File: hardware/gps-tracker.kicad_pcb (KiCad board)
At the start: 4 copper layers, 83 parts, among them J1 USB_B_Micro, J2 Conn_01x07, J3 Conn_01x08, J4 Conn_01x03, J5 Conn_01x04, SW1 SW_Push, SW2 SW_Push, SW3 SW_Push, SW4 SW_Push, SW5 SW_Push, SW6 SW_DPDT_x2, U1 STM32G070KBTx, U2 CH340C, U3 LTR-303ALS-01, U4 MIC5365-3.3YD5, U5 LIS2MDLTR, U6 LC86LICMD, U7 E22-900T30S, U8 TP4056

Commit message: First pass at PCB positions
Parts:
- removed H4: MountingHole, MountingHole:MountingHole_3.2mm_M3
- added C16: 470uF, Homebrew:CP_Radial_D6.3mm_P2.50mm_470uF, B.Cu at (123.1, 103.8)
- added C19: 470uF, Homebrew:CP_Radial_D6.3mm_P2.50mm_470uF, B.Cu at (122.8, 115.8)
- added C34: 10uF, Capacitor_SMD:C_0603_1608Metric, B.Cu at (131.7, 63.5)
- added C35: 10uF, Capacitor_SMD:C_0603_1608Metric, B.Cu at (85.8, 106.7)
- added C36: 100nF, Capacitor_SMD:C_0402_1005Metric, B.Cu at (137.3, 63.0)
- added C37: 47uF, Capacitor_SMD:C_1206_3216Metric, B.Cu at (143.7, 57.4)
- added C38: 470uF, Homebrew:CP_Radial_D6.3mm_P2.50mm_470uF, B.Cu at (133.5, 54.9)
- added D8: D_TVS, Diode_SMD:D_SOD-123F, B.Cu at (148.4, 57.4)
- added R22: 10k, Resistor_SMD:R_0402_1005Metric, B.Cu at (131.5, 61.4)
- added R23: 220, Resistor_SMD:R_0402_1005Metric, B.Cu at (140.0, 67.2)
- added R24: 220, Resistor_SMD:R_0402_1005Metric, B.Cu at (140.5, 65.3)
- added R25: 1k, Resistor_SMD:R_0402_1005Metric, B.Cu at (105.0, 106.1)
- added U9: MIC5365-3.3YD5, Package_TO_SOT_SMD:SOT-23-5, B.Cu at (134.7, 62.5)
- C1, C10, C11, C12, C13, C14, C15, C17, C18, C2, C20, C21, C22, C23, C24, C25, C26, C27, C28, C29, C3, C30, C32, C33, C4, C5, C6, C7, C8, C9, D1, D2, D6, D7, J1, J2, J4, J5, R1, R10, R11, R13, R15, R16, R17, R18, R19, R2, R20, R3, R4, R5, R6, R7, R8, R9, SW2, TH1, U1, U2, U4, U5, U8: moved to B.Cu
- D3, D4, D5: footprint Diode_SMD:D_SMB -> Diode_SMD:D_SOD-123F; moved to B.Cu
- R12, R14, R21: footprint Resistor_SMD:R_0402_1005Metric -> Resistor_SMD:R_0603_1608Metric; moved to B.Cu
- SW6: value SW_DPDT_x2 -> SW_SPDT; footprint Homebrew:SK22D15L5_SP -> Homebrew:SS-12D03-G5; moved to B.Cu
- U7: value E22-900T30S -> E22-900M22S; footprint Homebrew:XCVR_E22-900T30S -> Homebrew:E22-900M22S; moved to B.Cu
- moved C22 205.8 mm to (75.5, 65.7), turned to -90 degrees
- moved C31 204.2 mm to (74.2, 65.6), turned to 90 degrees
- moved C24 203.6 mm to (73.2, 65.6), turned to 90 degrees
- moved C29 203.2 mm to (74.2, 65.6), turned to 90 degrees
- moved C27 202.7 mm to (74.3, 69.0), turned to 90 degrees
- moved J2 185.3 mm to (99.6, 79.3), turned to -90 degrees
- moved C28 183.3 mm to (77.3, 69.5), turned to 180 degrees
- moved R17 181.4 mm to (100.4, 98.3), turned to 180 degrees
- moved R16 181.3 mm to (100.4, 99.9)
- moved C20 181.0 mm to (87.6, 104.6), turned to 180 degrees
- moved C17 181.0 mm to (87.1, 106.7), turned to -90 degrees
- moved C18 179.2 mm to (88.9, 108.4), turned to 180 degrees
- moved U6 179.1 mm to (84.0, 65.2)
- moved U5 177.1 mm to (89.0, 106.5), turned to 180 degrees
- moved U3 176.3 mm to (92.8, 114.8), turned to 180 degrees
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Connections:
- C23 pad 2: +BATT -> /RADIO_PWR
- C25 pad 1: +BATT -> /RADIO_PWR
- C30 pad 1: +BATT -> /RADIO_PWR
- SW2 pad 2: Net-(U1-NRST) -> Net-(R25-Pad1)
- SW6 pad 1: unconnected-(SW6A-A-Pad1) -> /BATT_DIRECT
- SW6 pad 2: /BATT_DIRECT -> +BATT
- SW6 pad 3: +BATT -> unconnected-(SW6-C-Pad3)
- U1 pad 2: /RADIO_M0 -> /RADIO_RXEN
- U1 pad 26: /RADIO_AUX -> unconnected-(U1-PA15-Pad26)
- U1 pad 3: /RADIO_M1 -> /RADIO_CS
- U1 pad 30: /RADIO_RXD -> /RADIO_DIO1
- U1 pad 31: /RADIO_TXD -> /RADIO_BUSY
- U7 pad 1: /RADIO_M0 -> GND
- U7 pad 10: (no net) -> GND
- U7 pad 11: (no net) -> GND
- U7 pad 12: (no net) -> GND
- U7 pad 13: (no net) -> /RADIO_DIO1
- U7 pad 14: (no net) -> /RADIO_BUSY
- U7 pad 15: GND -> unconnected-(U7-NRST-Pad15)
- U7 pad 16: GND -> /MISO
- U7 pad 17: GND -> /MOSI
- U7 pad 18: unconnected-(U7-ANT-Pad18) -> /SCK
- U7 pad 2: /RADIO_M1 -> GND
- U7 pad 3: /RADIO_RXD -> GND
- U7 pad 4: /RADIO_TXD -> GND
- U7 pad 5: /RADIO_AUX -> GND
- U7 pad 6: +BATT -> Net-(U7-RXEN)
- U7 pad 7: GND -> Net-(U7-TXEN)
- U7 pad 8: (no net) -> Net-(U7-DIO2)
- U7 pad 9: GND -> /RADIO_PWR
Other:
- board outline added: 87.6 x 80.9 mm

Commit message: Hardware v1.0
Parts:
- removed C13: 10uF, Capacitor_SMD:C_0603_1608Metric
- removed C38: 470uF, Homebrew:CP_Radial_D6.3mm_P2.50mm_470uF
- removed R9: 22, Resistor_SMD:R_0402_1005Metric
- added D9: D, Diode_SMD:D_SMA, B.Cu at (96.0, 117.1)
- added J6: Conn_01x03, Connector_PinHeader_2.54mm:PinHeader_1x03_P2.54mm_Vertical, B.Cu at (102.9, 85.3)
- added J7: Conn_01x02, Homebrew:JST_Micro_1x02_P1.25mm_Horizontal, B.Cu at (74.6, 106.5)
- C16, C19: value 470uF -> 220uF; footprint Homebrew:CP_Radial_D6.3mm_P2.50mm_470uF -> Capacitor_THT:CP_Radial_D10.0mm_P5.00mm
- C2: value 47pF -> 10uF; footprint Capacitor_SMD:C_0402_1005Metric -> Capacitor_SMD:C_0603_1608Metric
- C3: value 47pF -> 220uF; footprint Capacitor_SMD:C_0402_1005Metric -> Capacitor_THT:CP_Radial_D10.0mm_P5.00mm
- R2: value 3k3 -> 220; footprint Resistor_SMD:R_0603_1608Metric -> Resistor_SMD:R_0402_1005Metric
- R4: value 22 -> 4k7
- R6: value 22 -> 1k
- R8: value 22 -> 220
- TH1: footprint Fuse:Fuse_1812_4532Metric_Pad1.30x3.40mm_HandSolder -> Fuse:Fuse_0805_2012Metric
- U2: value CH340C -> CH340X; footprint Package_SO:SOIC-16_3.9x9.9mm_P1.27mm -> Package_SO:MSOP-10_3x3mm_P0.5mm
- moved D8 69.6 mm to (82.1, 78.5), turned to 180 degrees
- moved H1 64.3 mm to (84.9, 56.0)
- moved C17 62.5 mm to (146.6, 87.6)
- moved C20 62.5 mm to (147.3, 85.9)
- moved U5 62.4 mm to (148.5, 87.9)
- moved C18 62.4 mm to (148.5, 89.8)
- moved C35 62.4 mm to (145.3, 88.1)
- moved C3 61.7 mm to (84.5, 71.9), turned to 180 degrees
- moved J4 61.1 mm to (79.7, 116.9), turned to 0 degrees
- moved C37 57.0 mm to (87.2, 64.8), turned to -90 degrees
- moved C19 52.5 mm to (77.6, 89.2), turned to 90 degrees
- moved C36 51.9 mm to (85.4, 63.7)
- moved U9 51.9 mm to (82.8, 63.1)
- moved C25 51.9 mm to (88.1, 59.8)
- moved U7 51.8 mm to (90.7, 74.9)
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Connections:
- net /GPS_RXD renamed /GPS_TX
- net /GPS_TXD renamed /GPS_RX
- net /USART_TXD renamed /USART_RX
- C16 pad 1: VCC -> +BATT
- C19 pad 1: +BATT -> VCC
- C2 pad 1: /USB+ -> GND
- C2 pad 2: GND -> /BATT_DIRECT
- C3 pad 1: /USB- -> /RADIO_PWR
- D7 pad 2: Net-(D7-A) -> VBUS
- R2 pad 1: /BOOT0 -> Net-(U2-RXD)
- R2 pad 2: VBUS -> /USART_TX
- R21 pad 2: VCC -> Net-(J6-Pin_2)
- R4 pad 1: /USB+ -> Net-(U2-~{CTS})
- R4 pad 2: Net-(U2-UD+) -> /~{DTR}
- R6 pad 1: /USB- -> VBUS
- R6 pad 2: Net-(U2-UD-) -> Net-(U8-CE)
- SW6 pad 1: /BATT_DIRECT -> unconnected-(SW6-A-Pad1)
- SW6 pad 3: unconnected-(SW6-C-Pad3) -> /BATT_DIRECT
- U1 pad 2: /RADIO_RXEN -> /SW4
- U1 pad 20: /SW4 -> /RADIO_RXEN
- U1 pad 26: unconnected-(U1-PA15-Pad26) -> /RADIO_CS
- U1 pad 29: /SW1 -> /SW2
- U1 pad 3: /RADIO_CS -> unconnected-(U1-PC15-Pad3)
- U1 pad 7: /SW2 -> /SW1
- U1 pad 9: /USART_RXD -> /USART_TX
- U2 pad 1: GND -> /USB+
- U2 pad 10: unconnected-(U2-~{DSR}-Pad10) -> VCC
- U2 pad 2: Net-(U2-TXD) -> /USB-
- U2 pad 3: Net-(U2-RXD) -> GND
- U2 pad 4: VCC -> /BOOT0
- U2 pad 5: Net-(U2-UD+) -> Net-(U2-~{CTS})
- U2 pad 6: Net-(U2-UD-) -> /~{DTR}
- U2 pad 7: unconnected-(U2-NC-Pad7) -> VCC
- U2 pad 8: unconnected-(U2-NC-Pad8) -> Net-(U2-TXD)
- U2 pad 9: unconnected-(U2-~{CTS}-Pad9) -> Net-(U2-RXD)
- U8 pad 8: Net-(D7-A) -> Net-(U8-CE)
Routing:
- net GND: track 0.00 -> 166.7 mm, vias 0 -> 15
- net /SCK: track 0.00 -> 116.3 mm, vias 0 -> 4
- net /MOSI: track 0.00 -> 109.1 mm, vias 0 -> 3
- net +BATT: track 0.00 -> 108.2 mm, vias 0 -> 3
- net /MISO: track 0.00 -> 81.8 mm, vias 0 -> 3
- net VCC: track 0.00 -> 76.5 mm, vias 0 -> 12
- net /RADIO_BUSY: track 0.00 -> 62.2 mm, vias 0 -> 4
- net /RADIO_DIO1: track 0.00 -> 58.2 mm, vias 0 -> 4
- net /GPS_TX: track 0.00 -> 56.5 mm, vias 0 -> 5
- net /RADIO_RXEN: track 0.00 -> 55.6 mm, vias 0 -> 4
- net /BOOT0: track 0.00 -> 55.4 mm, vias 0 -> 5
- net /BATT_DIRECT: track 0.00 -> 51.3 mm, vias 0 -> 1
- net /SDA: track 0.00 -> 50.6 mm, vias 0 -> 6
- net /SCL: track 0.00 -> 50.4 mm, vias 0 -> 6
- net /COMPASS_CS: track 0.00 -> 48.7 mm, vias 0 -> 2
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- added copper zone on B.Cu, net GND
- added copper zone on F.Cu, net GND
- added copper zone on In1.Cu, net GND
- added copper zone on In2.Cu, net GND
- added copper zone on In1.Cu, net VCC
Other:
- board size 87.6 x 80.9 mm -> 84.9 x 74.8 mm
- board text added: "+"
- board text added: "-"
- board text added: "2Ah BATTERY"
- board text added: "3V3"
- board text added: "A1"
- board text added: "A2"
- board text added: "BAT"
- board text added: "BLK"
- board text added: "CHARGE"
- board text added: "CLK"
- board text added: "CS"
- board text added: "DC"
- board text added: "GND"
- board text added: "GPS_CLK"
- board text added: "IO"
- board text added: "MOSI"
- board text added: "OFF"
- board text added: "ON"
- board text added: "REG"
- board text added: "RESET"
- board text added: "SCK"
- board text added: "SCL"
- board text added: "SCREEN"
- board text added: "SDA"
- board text added: "gps-tracker v1.0"
- board text added: "~{RST}"

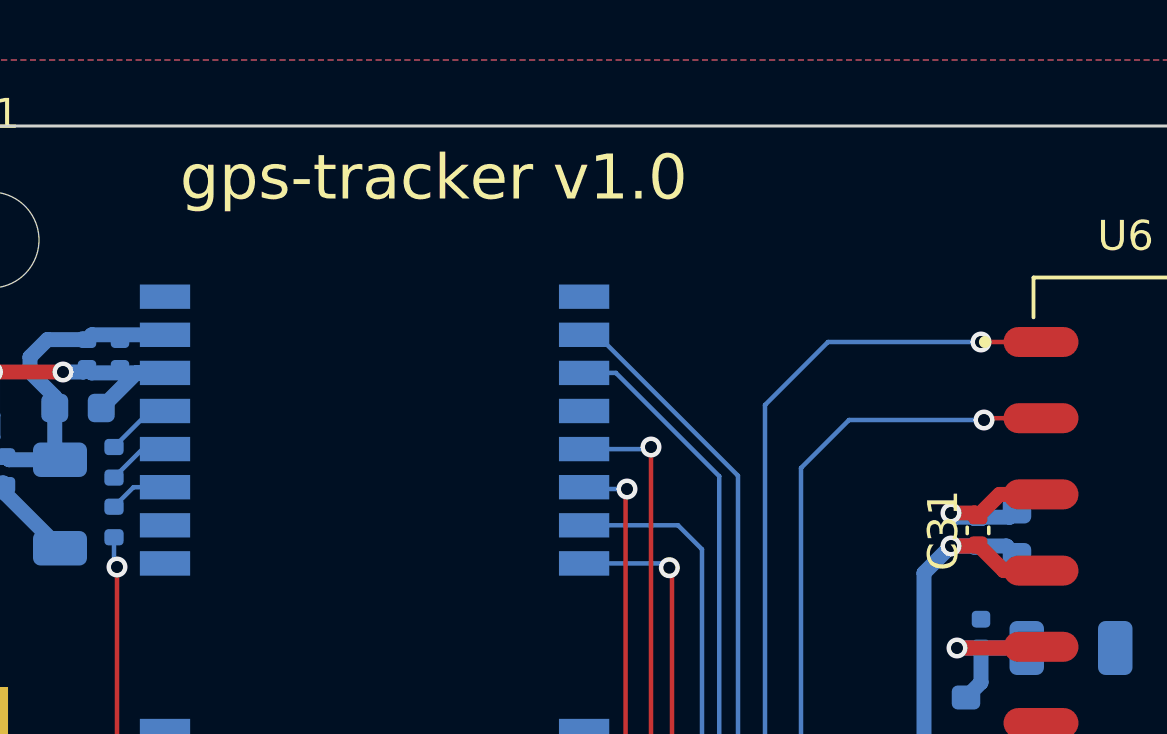
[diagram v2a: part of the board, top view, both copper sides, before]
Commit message: Some fixes for hardware v1.0
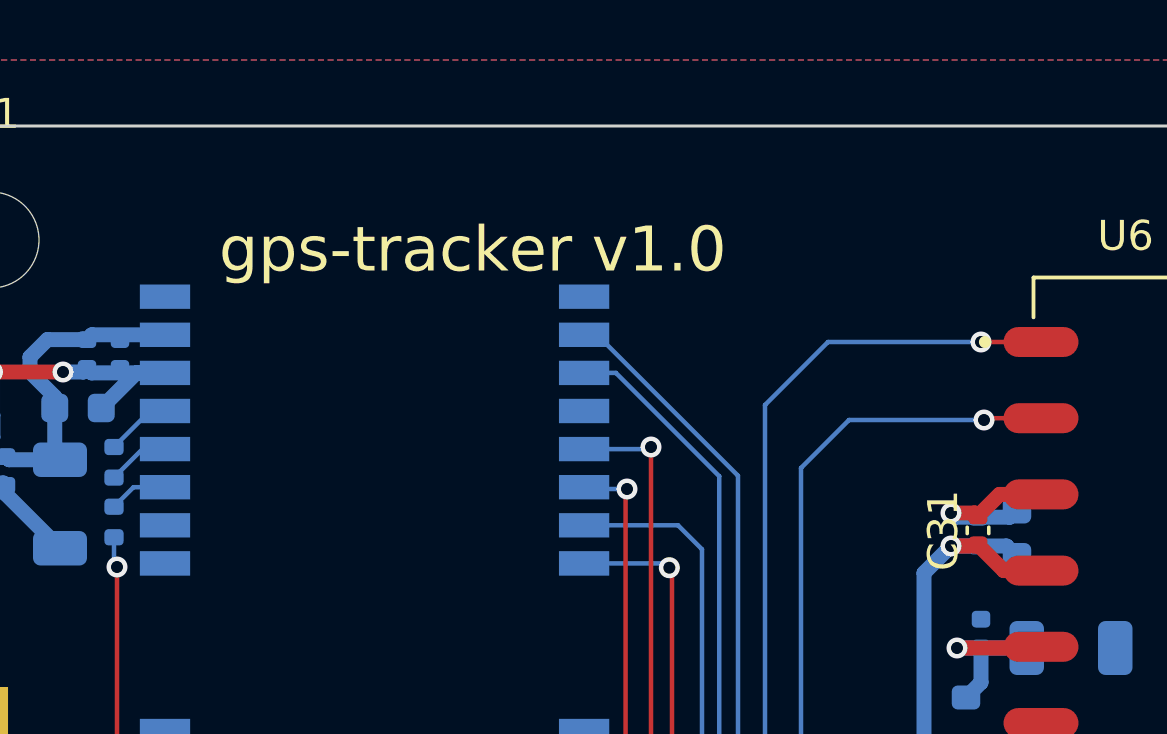
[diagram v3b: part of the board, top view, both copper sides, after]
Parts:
- removed C29: 100nF, Capacitor_SMD:C_0402_1005Metric
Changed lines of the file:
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@@
       (net 9 "/BATT_DIRECT") (pinfunction "C") (pintype "passive"))
   )
-  (footprint "Capacitor_SMD:C_0402_1005Metric" (layer "B.Cu")
-    (at 117.8 65.72 90)
-    (descr "Capacitor SMD 0402 (1005 Metric), square (rectangular) end terminal, IPC_7351 nominal, (Body size source: IPC-SM-782 page 76, https://www.pcb-3d.com/wordpress/wp-content/uploads/ipc-sm-782a_amendment_1_and_2.pdf), generated with kicad-footprint-generator")
-    (tags "capacitor")
-    (property "LCSC" "C307331")
-    (property "Sheetfile" "gps-tracker.kicad_sch")
-    (property "Sheetname" "")
-    (property "ki_description" "Unpolarized capacitor")
-    (property "ki_keywords" "cap capacitor")
-    (attr smd)
-    (fp_text reference "C29" (at 0 1.16 90) (layer "B.SilkS")
-        (effects (font (size 1 1) (thickness 0.15)) (justify mirror))
-    )
-    (fp_text value "100nF" (at 0 -1.16 90) (layer "B.Fab")
-        (effects (font (size 1 1) (thickness 0.15)) (justify mirror))
-    )
-    (fp_text user "${REFERENCE}" (at 0 0 90) (layer "B.Fab")
-        (effects (font (size 0.25 0.25) (thickness 0.04)) (justify mirror))
-    )
-    (fp_line (start -0.107836 -0.36) (end 0.107836 -0.36)
-      (stroke (width 0.12) (type solid)) (layer "B.SilkS"))
-    (fp_line (start -0.107836 0.36) (end 0.107836 0.36)
-      (stroke (width 0.12) (type solid)) (layer "B.SilkS"))
-    (fp_line (start -0.91 -0.46) (end -0.91 0.46)
-      (stroke (width 0.05) (type solid)) (layer "B.CrtYd"))
-    (fp_line (start -0.91 0.46) (end 0.91 0.46)
-      (stroke (width 0.05) (type solid)) (layer "B.CrtYd"))
-    (fp_line (start 0.91 -0.46) (end -0.91 -0.46)
-      (stroke (width 0.05) (type solid)) (layer "B.CrtYd"))
-    (fp_line (start 0.91 0.46) (end 0.91 -0.46)
-      (stroke (width 0.05) (type solid)) (layer "B.CrtYd"))
-    (fp_line (start -0.5 -0.25) (end -0.5 0.25)
-      (stroke (width 0.1) (type solid)) (layer "B.Fab"))
-    (fp_line (start -0.5 0.25) (end 0.5 0.25)
-      (stroke (width 0.1) (type solid)) (layer "B.Fab"))
-    (fp_line (start 0.5 -0.25) (end -0.5 -0.25)
-      (stroke (width 0.1) (type solid)) (layer "B.Fab"))
-    (fp_line (start 0.5 0.25) (end 0.5 -0.25)
-      (stroke (width 0.1) (type solid)) (layer "B.Fab"))
-    (pad "1" smd roundrect (at -0.48 0 90) (size 0.56 0.62) (layers "B.Cu" "B.Paste" "B.Mask") (roundrect_rratio 0.25)
-      (net 6 "VCC") (pintype "passive"))
-    (pad "2" smd roundrect (at 0.48 0 90) (size 0.56 0.62) (layers "B.Cu" "B.Paste" "B.Mask") (roundrect_rratio 0.25)
-      (net 4 "GND") (pintype "passive"))
-    (model "${KICAD7_3DMODEL_DIR}/Capacitor_SMD.3dshapes/C_0402_1005Metric.wrl"
-      (offset (xyz 0 0 0))
-      (scale (xyz 1 1 1))
-      (rotate (xyz 0 0 0))
-    )
-  )
   (footprint "Resistor_SMD:R_0402_1005Metric" (layer "B.Cu")
     (at 108.3 117.39 90)
@@
     (effects (font (size 1 1) (thickness 0.15)) (justify left bottom))
   )
-  (gr_text "gps-tracker v1.0" (at 91.2 54.8) (layer "F.SilkS")
+  (gr_text "gps-tracker v1.0" (at 92.5 57.2) (layer "F.SilkS")
     (effects (font (size 1.5 1.5) (thickness 0.2)) (justify left bottom))
   )
